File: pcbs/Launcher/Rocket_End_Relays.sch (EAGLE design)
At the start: 39 parts, among them IC2 LM2576T-ADJ, K4 LD105, K5 LD105, K6 LD105, K7 LD105, T1 BC547, T2 BC547, T3 BC547, T4 BC547, T5 BC547, U1 ARDUINO-MEGAPRO-5V, X2 22-23-2041, X3 22-23-2021

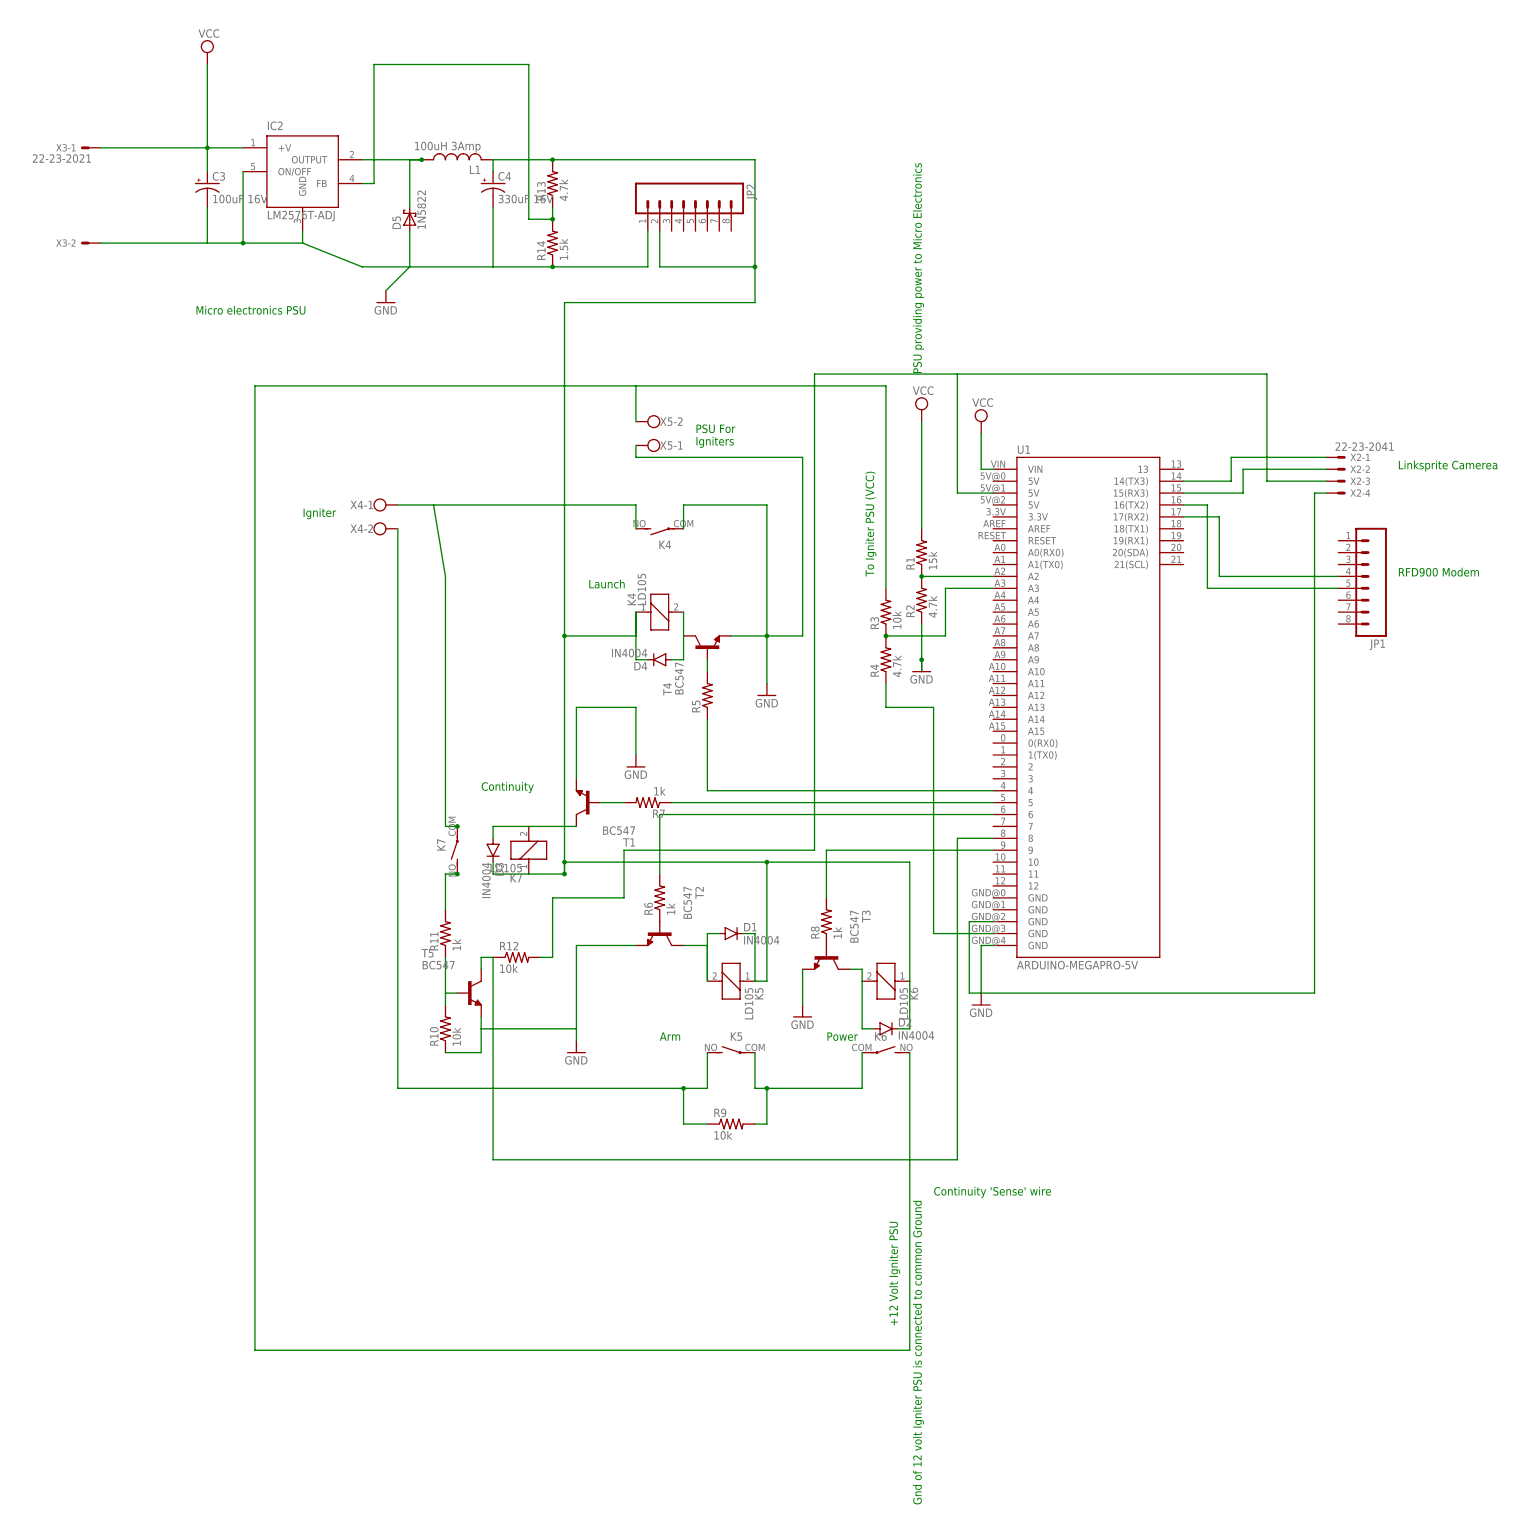
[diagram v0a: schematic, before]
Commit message: * Correcting the right-angle connector tracks for a RFD900p module connected logo up. Also made sure it was 10mm from the edge of the pdb * Put in correct 2 pin screw terminal blocks with pitch of 3.5mm
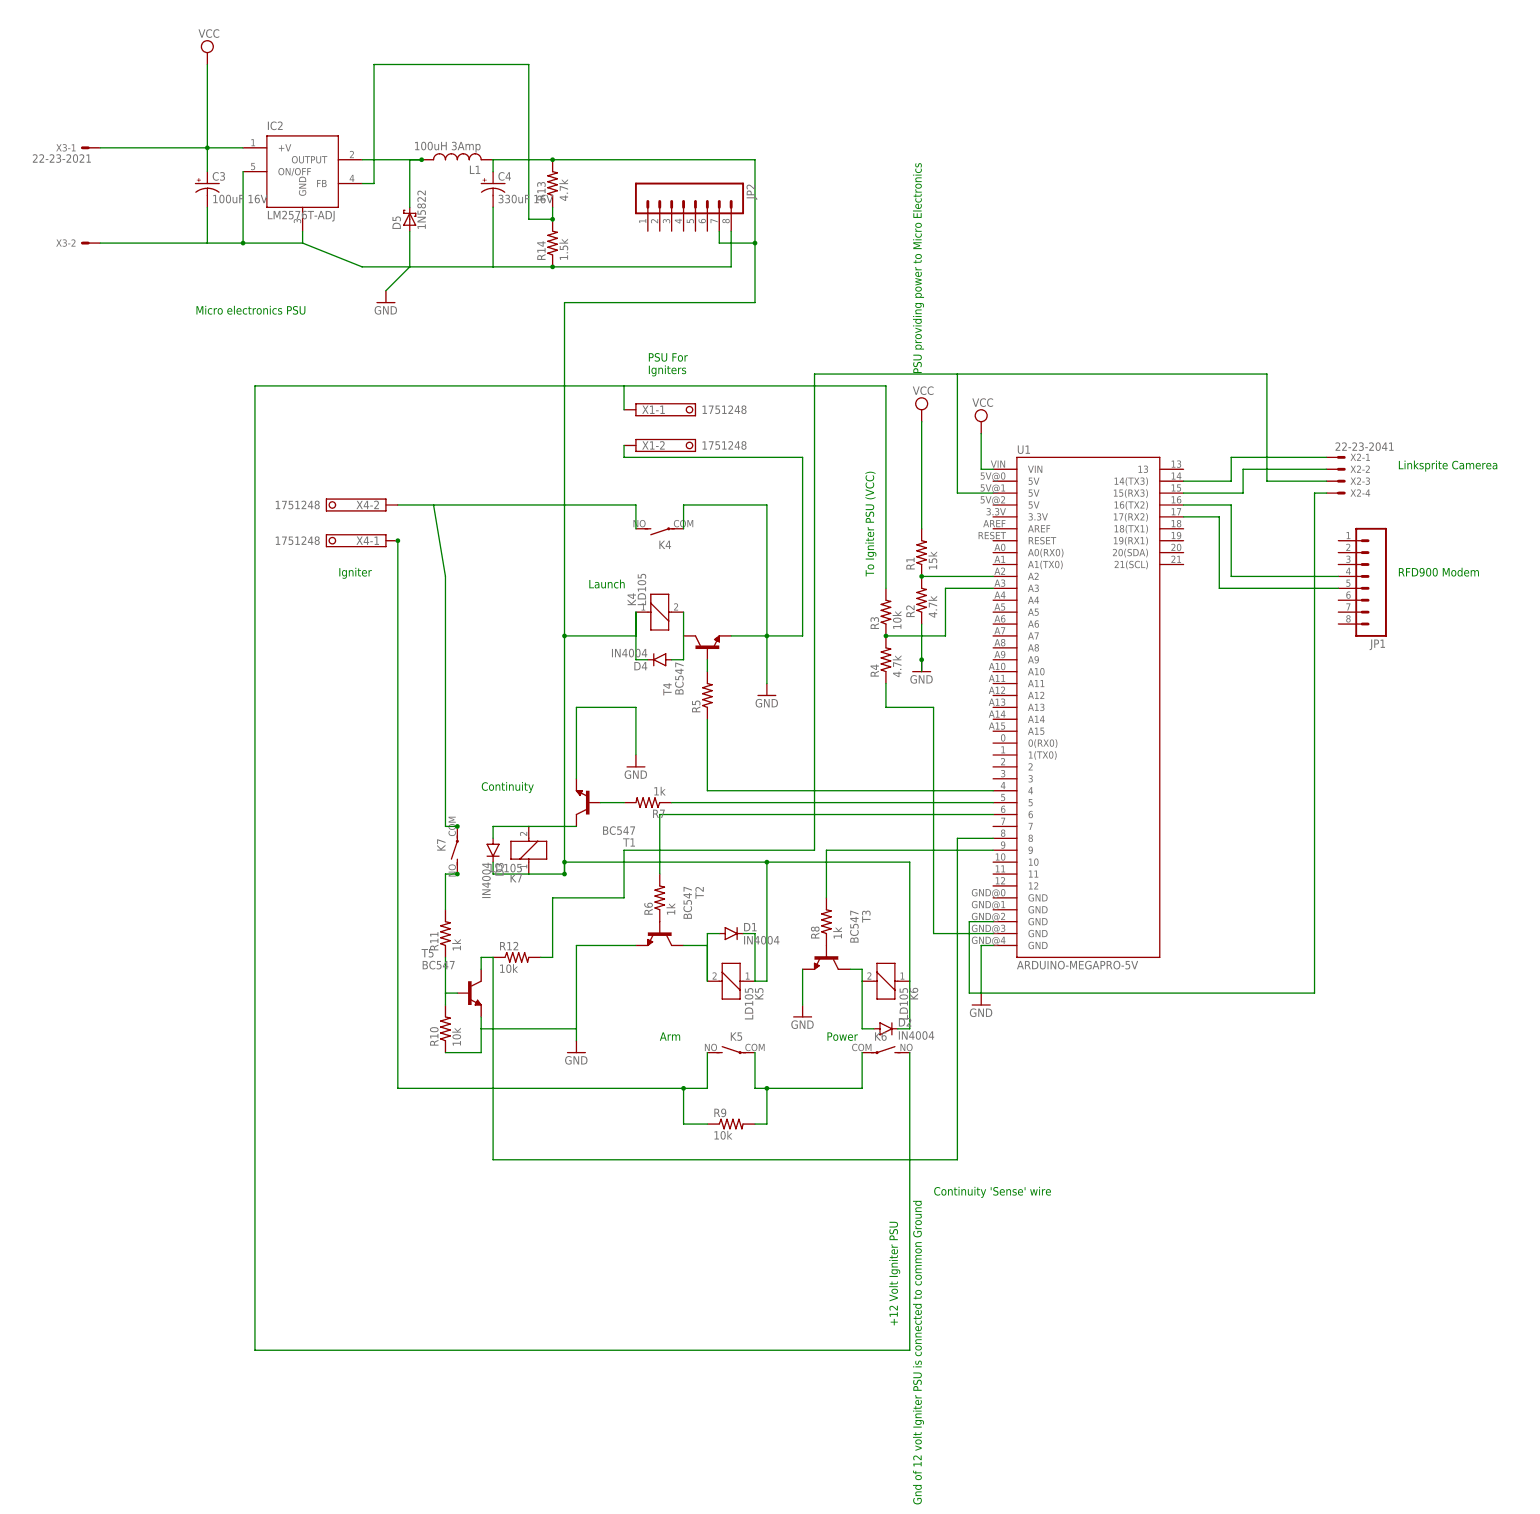
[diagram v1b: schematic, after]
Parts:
- removed X5: (no value), con-wago-500:W237-102
- added X1: 1751248, con-phoenix-350:1751248
- X4: value (none) -> 1751248; device con-wago-500:W237-102 -> con-phoenix-350:1751248
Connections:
- net N$1: now also JP1.4; no longer JP1.5
- net N$15: now also X4-2.K; no longer X4-1.KL
- net N$17: now also X4-1.K; no longer X4-2.KL
- net N$2: now also JP1.5; no longer JP1.4
- net N$29: now also X1-1.K; no longer X5-2.KL
- net N$33: now also JP2.8, X1-2.K; no longer JP2.1, X5-1.KL
- net N$5: now also JP2.7; no longer JP2.2
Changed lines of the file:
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@@
 <part name="SUPPLY2" library="supply2" deviceset="VCC" device=""/>
 <part name="R10" library="rcl" deviceset="R-US_" device="0207/7" value="10k"/>
-<part name="X5" library="con-wago-500" deviceset="W237-102" device=""/>
-<part name="X4" library="con-wago-500" deviceset="W237-102" device=""/>
 <part name="JP1" library="SparkFun-Connectors" deviceset="M08" device=""/>
 <part name="JP2" library="SparkFun-Connectors" deviceset="M08" device=""/>
+<part name="X1" library="con-phoenix-350" deviceset="1751248" device=""/>
+<part name="X4" library="con-phoenix-350" deviceset="1751248" device=""/>
 </parts>
 <sheets>
@@
 <text x="-91.44" y="35.56" size="1.778" layer="91">Continuity</text>
 <text x="5.08" y="-50.8" size="1.778" layer="91">Continuity 'Sense' wire</text>
-<text x="-129.54" y="93.98" size="1.778" layer="91">Igniter</text>
+<text x="-121.92" y="81.28" size="1.778" layer="91">Igniter</text>
 <text x="-2.54" y="-78.74" size="1.778" layer="91" rot="R90">+12 Volt Igniter PSU</text>
 <text x="2.54" y="-116.84" size="1.778" layer="91" rot="R90">Gnd of 12 volt Igniter PSU is connected to common Ground</text>
 <text x="2.54" y="124.46" size="1.778" layer="91" rot="R90">PSU providing power to Micro Electronics</text>
-<text x="-45.72" y="109.22" size="1.778" layer="91">PSU For
+<text x="-55.88" y="124.46" size="1.778" layer="91">PSU For
 Igniters</text>
 <text x="-152.4" y="137.16" size="1.778" layer="91">Micro electronics PSU</text>
@@
 <instance part="SUPPLY2" gate="G$1" x="-149.86" y="193.04"/>
 <instance part="R10" gate="G$1" x="-99.06" y="-15.24" rot="R90"/>
-<instance part="X5" gate="-1" x="-53.34" y="109.22" rot="R180"/>
-<instance part="X5" gate="-2" x="-53.34" y="114.3" rot="R180"/>
-<instance part="X4" gate="-1" x="-114.3" y="96.52"/>
-<instance part="X4" gate="-2" x="-114.3" y="91.44"/>
 <instance part="JP1" gate="G$1" x="96.52" y="81.28" rot="R180"/>
 <instance part="JP2" gate="G$1" x="-48.26" y="160.02" rot="R270"/>
+<instance part="X1" gate="-1" x="-58.42" y="116.84"/>
+<instance part="X1" gate="-2" x="-58.42" y="109.22"/>
+<instance part="X4" gate="-1" x="-111.76" y="88.9" rot="R180"/>
+<instance part="X4" gate="-2" x="-111.76" y="96.52" rot="R180"/>
 </instances>
 <busses>
@@
 </segment>
 <segment>
-<wire x1="-58.42" y1="109.22" x2="-58.42" y2="106.68" width="0.1524" layer="91"/>
-<wire x1="-58.42" y1="106.68" x2="-22.86" y2="106.68" width="0.1524" layer="91"/>
+<wire x1="-60.96" y1="109.22" x2="-60.96" y2="106.68" width="0.1524" layer="91"/>
+<wire x1="-60.96" y1="106.68" x2="-22.86" y2="106.68" width="0.1524" layer="91"/>
 <wire x1="-22.86" y1="106.68" x2="-22.86" y2="68.58" width="0.1524" layer="91"/>
 <pinref part="T4" gate="G$1" pin="E"/>
@@
 <pinref part="K4" gate="2" pin="P"/>
 <wire x1="-22.86" y1="68.58" x2="-30.48" y2="68.58" width="0.1524" layer="91"/>
-<pinref part="X5" gate="-1" pin="KL"/>
+<pinref part="X1" gate="-2" pin="K"/>
 </segment>
 <segment>
@@
 <wire x1="-106.68" y1="154.94" x2="-106.68" y2="147.32" width="0.1524" layer="91"/>
 <wire x1="-88.9" y1="147.32" x2="-76.2" y2="147.32" width="0.1524" layer="91"/>
-<wire x1="-76.2" y1="147.32" x2="-55.88" y2="147.32" width="0.1524" layer="91"/>
+<wire x1="-76.2" y1="147.32" x2="-38.1" y2="147.32" width="0.1524" layer="91"/>
 <pinref part="C3" gate="G$1" pin="-"/>
 <wire x1="-149.86" y1="160.02" x2="-149.86" y2="152.4" width="0.1524" layer="91"/>
@@
 <pinref part="IC2" gate="G$1" pin="GND"/>
 <wire x1="-129.54" y1="152.4" x2="-129.54" y2="154.94" width="0.1524" layer="91"/>
-<pinref part="JP2" gate="G$1" pin="1"/>
-<wire x1="-55.88" y1="154.94" x2="-55.88" y2="147.32" width="0.1524" layer="91"/>
+<pinref part="JP2" gate="G$1" pin="8"/>
+<wire x1="-38.1" y1="147.32" x2="-38.1" y2="154.94" width="0.1524" layer="91"/>
 </segment>
 </net>
@@
 <pinref part="K7" gate="2" pin="P"/>
 <junction x="-96.52" y="27.94"/>
-<pinref part="X4" gate="-1" pin="KL"/>
+<pinref part="X4" gate="-2" pin="K"/>
 </segment>
 </net>
@@
 <wire x1="-48.26" y1="-35.56" x2="-48.26" y2="-27.94" width="0.1524" layer="91"/>
 <junction x="-48.26" y="-27.94"/>
-<wire x1="-109.22" y1="91.44" x2="-109.22" y2="-27.94" width="0.1524" layer="91"/>
 <pinref part="K5" gate="2" pin="S"/>
+<wire x1="-109.22" y1="88.9" x2="-109.22" y2="-27.94" width="0.1524" layer="91"/>
 <wire x1="-43.18" y1="-27.94" x2="-43.18" y2="-20.32" width="0.1524" layer="91"/>
-<pinref part="X4" gate="-2" pin="KL"/>
+<pinref part="X4" gate="-1" pin="K"/>
+<junction x="-109.22" y="88.9"/>
 </segment>
 </net>
@@
 <wire x1="0" y1="-83.82" x2="-139.7" y2="-83.82" width="0.1524" layer="91"/>
 <wire x1="-139.7" y1="-83.82" x2="-139.7" y2="121.92" width="0.1524" layer="91"/>
-<wire x1="-139.7" y1="121.92" x2="-58.42" y2="121.92" width="0.1524" layer="91"/>
+<wire x1="-139.7" y1="121.92" x2="-60.96" y2="121.92" width="0.1524" layer="91"/>
 <pinref part="R3" gate="G$1" pin="2"/>
-<wire x1="-58.42" y1="121.92" x2="-5.08" y2="121.92" width="0.1524" layer="91"/>
+<wire x1="-60.96" y1="121.92" x2="-5.08" y2="121.92" width="0.1524" layer="91"/>
 <wire x1="-5.08" y1="121.92" x2="-5.08" y2="78.74" width="0.1524" layer="91"/>
-<wire x1="-58.42" y1="114.3" x2="-58.42" y2="121.92" width="0.1524" layer="91"/>
+<wire x1="-60.96" y1="116.84" x2="-60.96" y2="121.92" width="0.1524" layer="91"/>
 <pinref part="K6" gate="2" pin="S"/>
-<pinref part="X5" gate="-2" pin="KL"/>
+<pinref part="X1" gate="-1" pin="K"/>
 </segment>
 </net>
@@
 <segment>
 <pinref part="U1" gate="G$1" pin="16(TX2)"/>
-<wire x1="63.5" y1="78.74" x2="63.5" y2="96.52" width="0.1524" layer="91"/>
-<wire x1="63.5" y1="96.52" x2="58.42" y2="96.52" width="0.1524" layer="91"/>
-<pinref part="JP1" gate="G$1" pin="5"/>
-<wire x1="63.5" y1="78.74" x2="91.44" y2="78.74" width="0.1524" layer="91"/>
+<wire x1="68.58" y1="81.28" x2="68.58" y2="96.52" width="0.1524" layer="91"/>
+<wire x1="68.58" y1="96.52" x2="58.42" y2="96.52" width="0.1524" layer="91"/>
+<pinref part="JP1" gate="G$1" pin="4"/>
+<wire x1="68.58" y1="81.28" x2="91.44" y2="81.28" width="0.1524" layer="91"/>
 </segment>
 </net>
@@
 <pinref part="U1" gate="G$1" pin="17(RX2)"/>
 <wire x1="58.42" y1="93.98" x2="66.04" y2="93.98" width="0.1524" layer="91"/>
-<wire x1="66.04" y1="93.98" x2="66.04" y2="81.28" width="0.1524" layer="91"/>
-<pinref part="JP1" gate="G$1" pin="4"/>
-<wire x1="66.04" y1="81.28" x2="91.44" y2="81.28" width="0.1524" layer="91"/>
+<wire x1="66.04" y1="93.98" x2="66.04" y2="78.74" width="0.1524" layer="91"/>
+<pinref part="JP1" gate="G$1" pin="5"/>
+<wire x1="66.04" y1="78.74" x2="91.44" y2="78.74" width="0.1524" layer="91"/>
 </segment>
 </net>
@@
 <wire x1="0" y1="-15.24" x2="-2.54" y2="-15.24" width="0.1524" layer="91"/>
 <wire x1="-73.66" y1="139.7" x2="-33.02" y2="139.7" width="0.1524" layer="91"/>
-<wire x1="-33.02" y1="139.7" x2="-33.02" y2="147.32" width="0.1524" layer="91"/>
-<wire x1="-33.02" y1="147.32" x2="-33.02" y2="170.18" width="0.1524" layer="91"/>
+<wire x1="-33.02" y1="139.7" x2="-33.02" y2="152.4" width="0.1524" layer="91"/>
+<wire x1="-33.02" y1="152.4" x2="-33.02" y2="170.18" width="0.1524" layer="91"/>
 <wire x1="-33.02" y1="170.18" x2="-76.2" y2="170.18" width="0.1524" layer="91"/>
 <pinref part="L1" gate="G$1" pin="2"/>
@@
 <pinref part="R13" gate="G$1" pin="2"/>
 <junction x="-76.2" y="170.18"/>
-<wire x1="-53.34" y1="147.32" x2="-33.02" y2="147.32" width="0.1524" layer="91"/>
-<junction x="-33.02" y="147.32"/>
-<pinref part="JP2" gate="G$1" pin="2"/>
-<wire x1="-53.34" y1="147.32" x2="-53.34" y2="154.94" width="0.1524" layer="91"/>
-</segment>
-</net>
+<wire x1="-33.02" y1="152.4" x2="-40.64" y2="152.4" width="0.1524" layer="91"/>
+<pinref part="JP2" gate="G$1" pin="7"/>
+<wire x1="-40.64" y1="152.4" x2="-40.64" y2="154.94" width="0.1524" layer="91"/>
+<junction x="-33.02" y="152.4"/>
+</segment>
+</net>

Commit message: * various updates to pcbs
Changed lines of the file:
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@@
 <pinref part="X2" gate="-4" pin="S"/>
 <wire x1="88.9" y1="99.06" x2="86.36" y2="99.06" width="0.1524" layer="91"/>
-<wire x1="86.36" y1="99.06" x2="86.36" y2="-7.62" width="0.1524" layer="91"/>
-<wire x1="86.36" y1="-7.62" x2="12.7" y2="-7.62" width="0.1524" layer="91"/>
-<wire x1="12.7" y1="-7.62" x2="12.7" y2="7.62" width="0.1524" layer="91"/>
+<wire x1="86.36" y1="99.06" x2="86.36" y2="-15.24" width="0.1524" layer="91"/>
+<wire x1="86.36" y1="-15.24" x2="12.7" y2="-15.24" width="0.1524" layer="91"/>
+<wire x1="12.7" y1="-15.24" x2="12.7" y2="7.62" width="0.1524" layer="91"/>
 <wire x1="12.7" y1="7.62" x2="17.78" y2="7.62" width="0.1524" layer="91"/>
 <pinref part="U1" gate="G$1" pin="GND@2"/>
@@
 </sheet>
 </sheets>
+<errors>
+</errors>
 </schematic>
 </drawing>

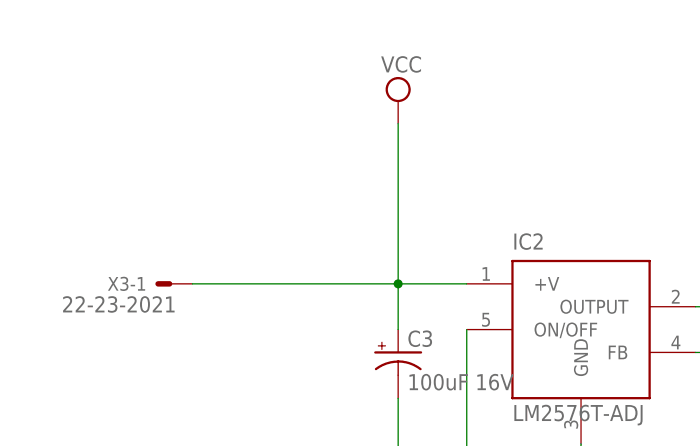
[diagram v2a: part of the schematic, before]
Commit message: * Widened some tracks * Put 2 x 2-pin connector for 7.4 PSU and Switch.
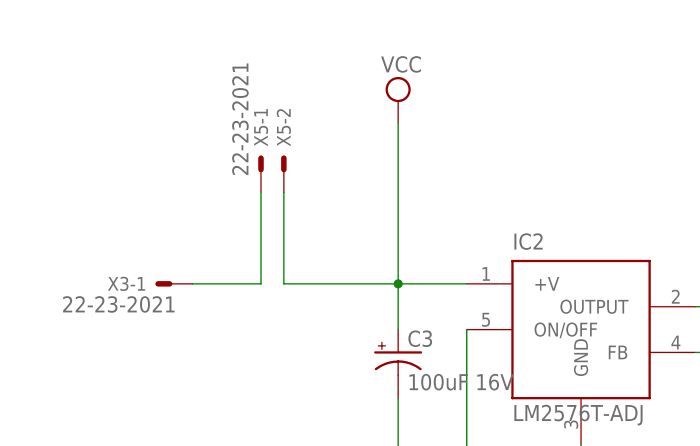
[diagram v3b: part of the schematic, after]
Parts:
- added X5: 22-23-2021, con-molex:22-23-2021
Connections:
- new net N$18: X3-1.S, X5-1.S
- net VCC: now also X5-2.S; no longer X3-1.S
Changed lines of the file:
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@@
 <part name="X1" library="con-phoenix-350" deviceset="1751248" device=""/>
 <part name="X4" library="con-phoenix-350" deviceset="1751248" device=""/>
+<part name="X5" library="con-molex" deviceset="22-23-2021" device=""/>
 </parts>
 <sheets>
@@
 <instance part="X4" gate="-1" x="-111.76" y="88.9" rot="R180"/>
 <instance part="X4" gate="-2" x="-111.76" y="96.52" rot="R180"/>
+<instance part="X5" gate="-1" x="-165.1" y="185.42" rot="R90"/>
+<instance part="X5" gate="-2" x="-162.56" y="185.42" rot="R90"/>
 </instances>
 <busses>
@@
 <pinref part="SUPPLY2" gate="G$1" pin="VCC"/>
 <wire x1="-149.86" y1="172.72" x2="-149.86" y2="190.5" width="0.1524" layer="91"/>
-<pinref part="X3" gate="-1" pin="S"/>
-<wire x1="-149.86" y1="172.72" x2="-172.72" y2="172.72" width="0.1524" layer="91"/>
+<pinref part="X5" gate="-2" pin="S"/>
+<wire x1="-162.56" y1="182.88" x2="-162.56" y2="172.72" width="0.1524" layer="91"/>
+<wire x1="-162.56" y1="172.72" x2="-149.86" y2="172.72" width="0.1524" layer="91"/>
 </segment>
 </net>
@@
 </segment>
 </net>
+<net name="N$18" class="0">
+<segment>
+<pinref part="X5" gate="-1" pin="S"/>
+<wire x1="-165.1" y1="182.88" x2="-165.1" y2="172.72" width="0.1524" layer="91"/>
+<pinref part="X3" gate="-1" pin="S"/>
+<wire x1="-165.1" y1="172.72" x2="-172.72" y2="172.72" width="0.1524" layer="91"/>
+</segment>
+</net>
